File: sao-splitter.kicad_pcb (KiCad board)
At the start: 2 copper layers, 66 x 47.3 mm, 7 parts

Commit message: Make smaller
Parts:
- J2, J3: footprint Library:IDC-Header_2x03_P2.54mm_Vertical_SilkscreenHidden -> Connector_PinSocket_2.54mm:PinSocket_2x03_P2.54mm_Vertical; moved to F.Cu
- R1, R2, R3, R4: value 330 -> 330Ω
- moved J2 9.54 mm to (152.4, 109.2), turned to 90 degrees
- moved J3 9.36 mm to (192.4, 109.0), turned to 90 degrees
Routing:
- net /SDA: track 85.9 -> 61.9 mm
- net /SCL: track 87.7 -> 68.8 mm
- net Net-(J2-Pin_6): track 24.2 -> 14.2 mm
- net Net-(J2-Pin_5): track 21.7 -> 11.7 mm
- net Net-(J3-Pin_6): track 26.3 -> 19.5 mm
- net Net-(J3-Pin_5): track 23.8 -> 17.3 mm
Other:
- board size 66 x 47.3 mm -> 50 x 32 mm
- board text added: "GPIO1"
- board text added: "GPIO2"
- board text added: "https://github.com/bwasserm/ sao-spectator-splitter"
- board text removed: "https://github.com/bwasserm/sao-spectator-splitter"

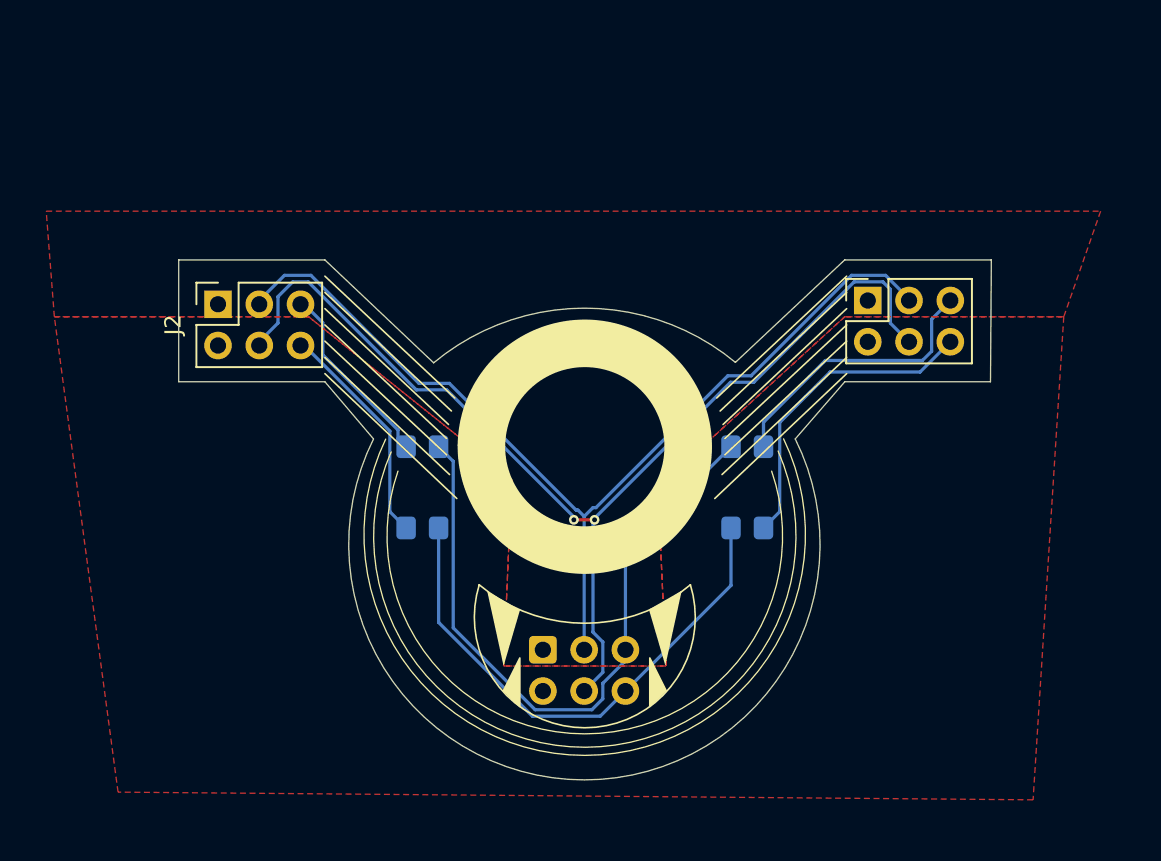
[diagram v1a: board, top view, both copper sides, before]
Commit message: Add 2 more eyestalks. Add README, license, and OSHW logo.
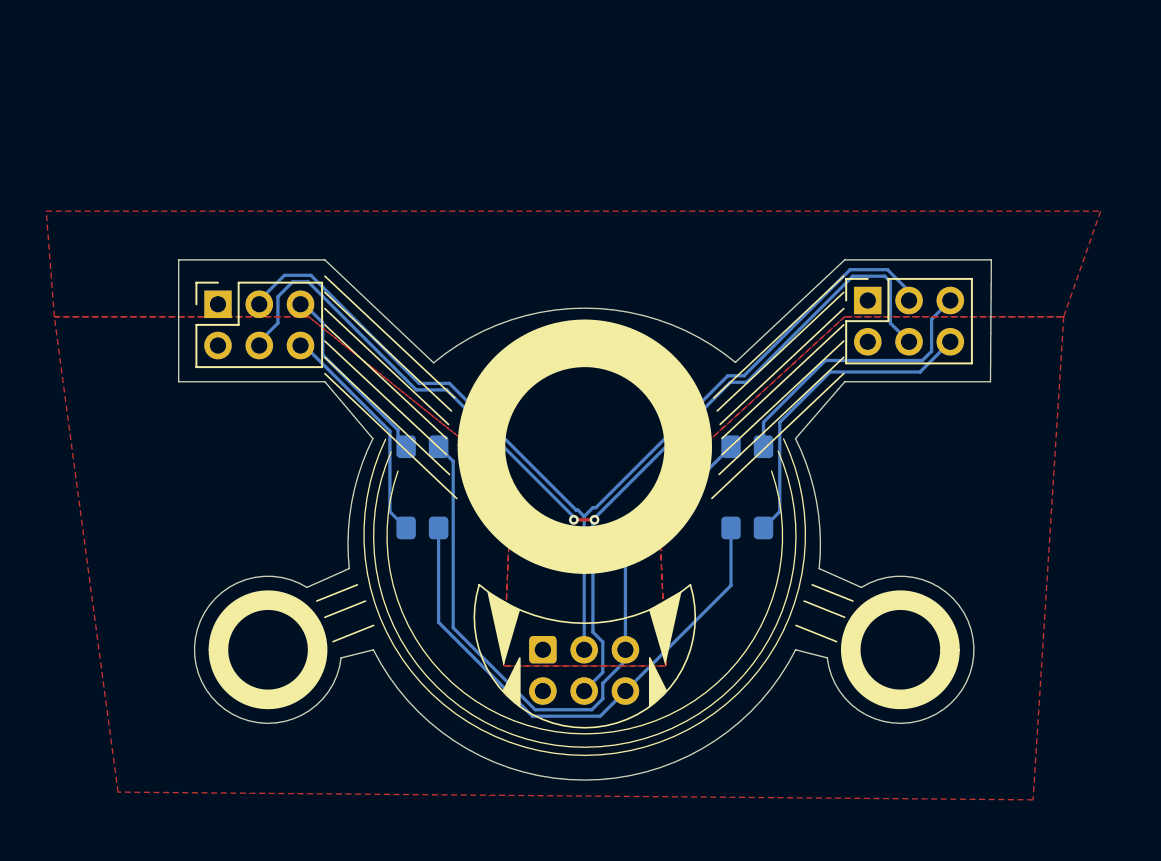
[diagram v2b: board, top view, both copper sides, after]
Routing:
- net /SDA: track 61.9 -> 62.4 mm
- net /SCL: track 68.8 -> 69.4 mm
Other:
- outline, holes or cut-outs redrawn
- board text added: "GP1 SDA 3.3V GP2 SCL GND"
- board text added: "Warning: input may only supply up to 250mA"

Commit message: More silkscreen updates
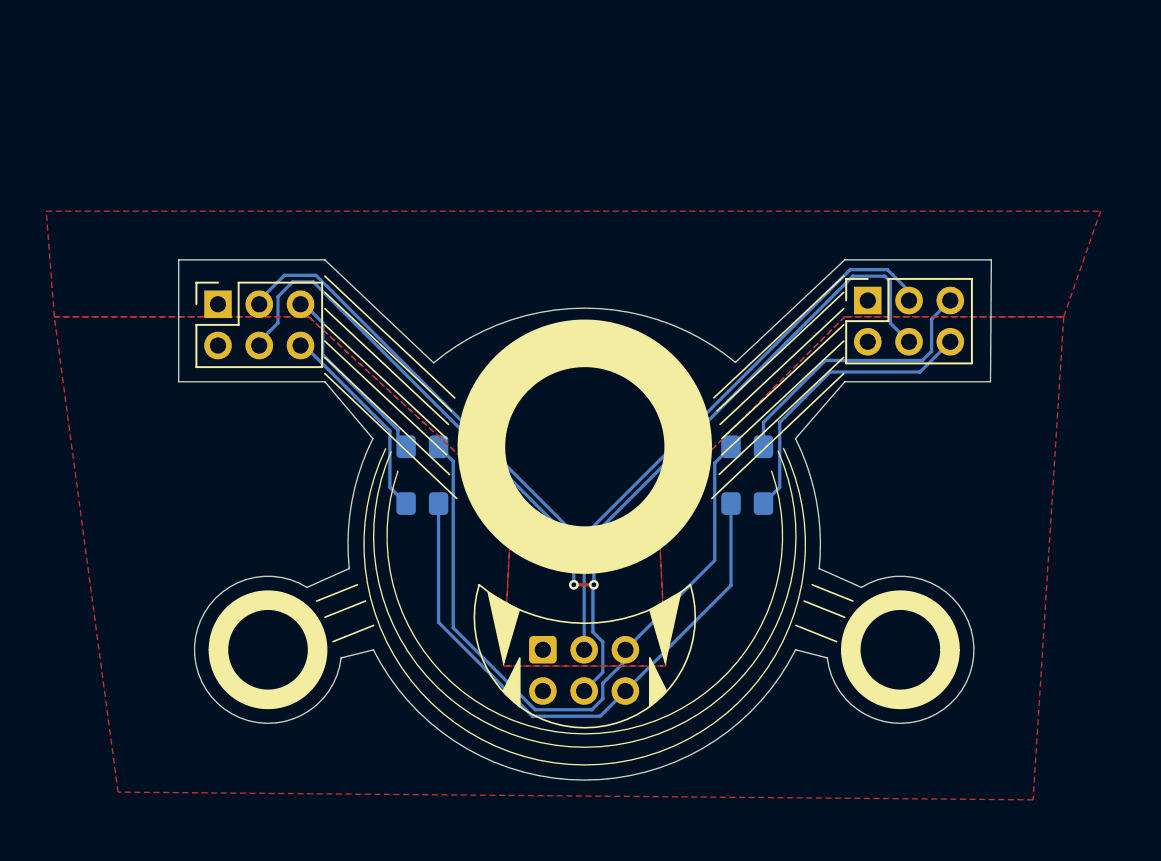
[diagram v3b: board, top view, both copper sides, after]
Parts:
- R4: value 330Ω -> All R's are rec 330Ω to isolate multiple SAOs' GPIOs from each other
- moved R2 1.50 mm to (165.0, 121.5)
- moved R4 1.50 mm to (185.0, 121.5)
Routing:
- net /GP2: track 33.1 -> 36.1 mm
- net /SCL: track 69.4 -> 71.9 mm
- net Net-(J2-Pin_6): track 14.2 -> 12.7 mm
- net Net-(J3-Pin_6): track 19.5 -> 18.0 mm
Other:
- board text added: "3.3V"
- board text added: "GND"
- board text added: "Isolate GPIOs by populating 330Ω to R's"
- board text added: "SAO Spectator Splitter v1"
- board text removed: "SAO Spectator Splitter"
